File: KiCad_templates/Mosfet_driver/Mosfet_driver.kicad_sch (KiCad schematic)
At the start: 22 parts, among them J1 KLS S1G03C, J2 KLS S1G03C, J3 KLS S1G03C, J4 KLS S1G02C, J5 KLS S1G02C

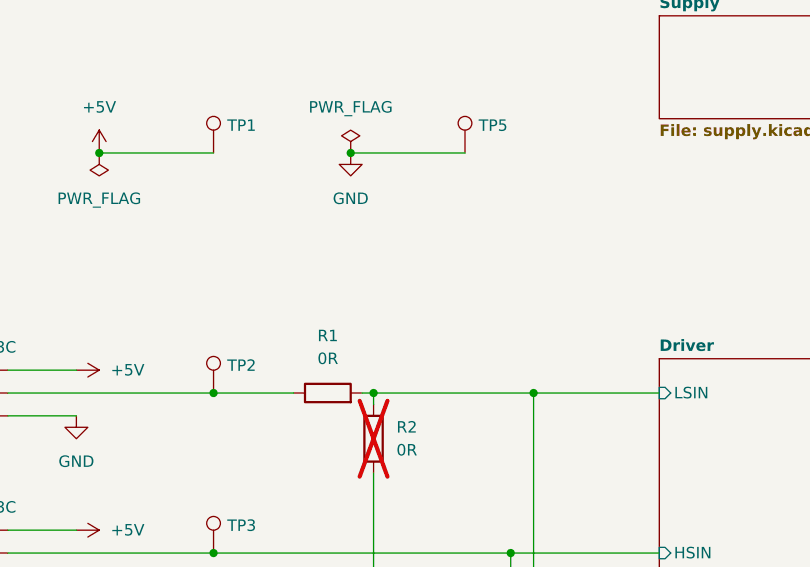
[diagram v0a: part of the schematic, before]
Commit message: Doplnen text do schematu a na dps
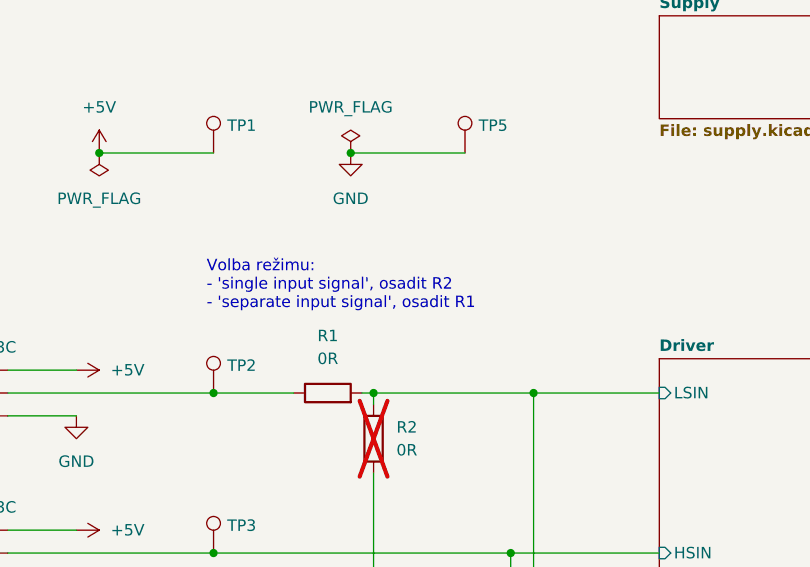
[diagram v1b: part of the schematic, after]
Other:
- note added: "Volba režimu: - 'single input signal', osadit R2 - 'separate input signal', osadit R1"
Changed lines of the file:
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@@
 		(rev "${REVISION}")
+	)
+	(text "Volba režimu:\n- 'single input signal', osadit R2\n- 'separate input signal', osadit R1"
+		(exclude_from_sim no)
+		(at 67.818 54.102 0)
+		(effects
+			(font
+				(size 1.27 1.27)
+			)
+			(justify left)
+		)
 	)
 	(junction
